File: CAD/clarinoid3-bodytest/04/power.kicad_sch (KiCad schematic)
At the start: 19 parts, among them IC2 Injoinic IP5306 battery charge, U7 TLV75733PDBV

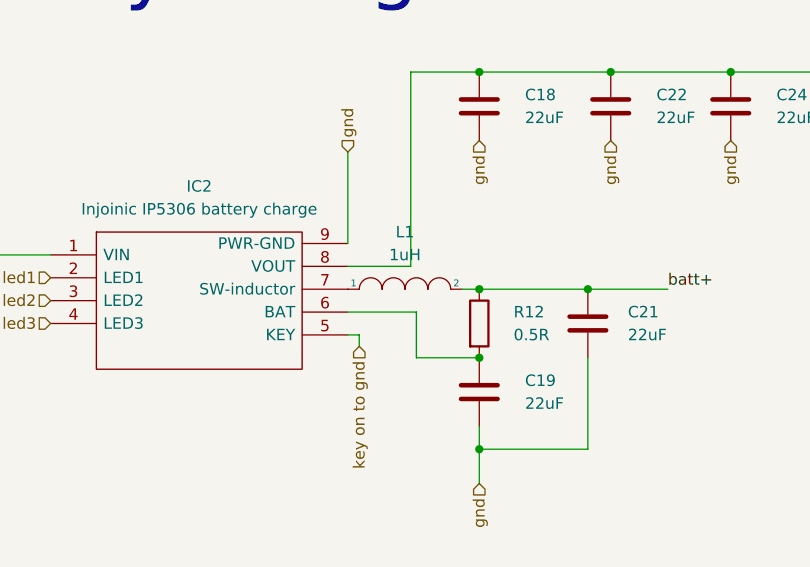
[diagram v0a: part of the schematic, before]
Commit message: c3 design work adding more 3dp tests
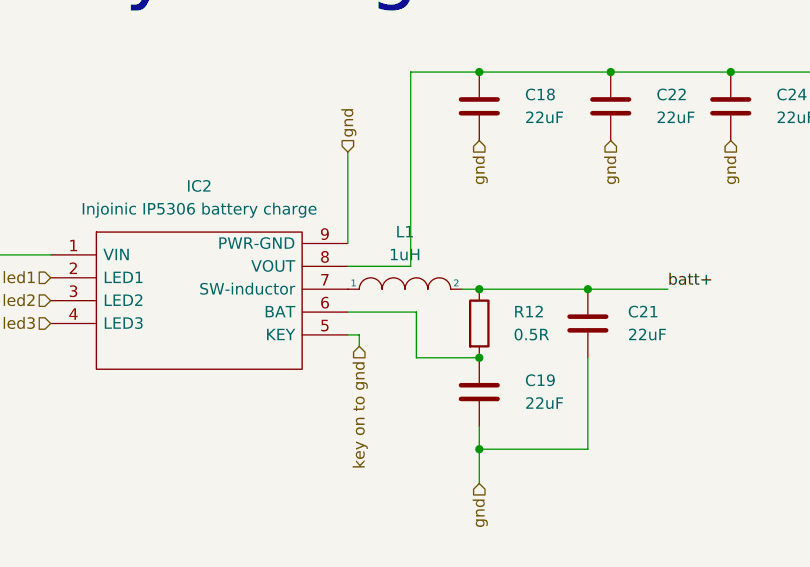
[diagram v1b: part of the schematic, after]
